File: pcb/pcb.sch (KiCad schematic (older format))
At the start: 19 parts

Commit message: Improved schematic
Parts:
- added C?: 100n, symbol Device:C
- added D?: D, symbol Device:D
- added J?: BAT+, symbol Connector:Conn_01x01_Male
- added J?: BAT-, symbol Connector:Conn_01x01_Male
- added R?: 330, symbol Device:R
- added R?: 2.7K, symbol Device:R
- added U?: AP9101CK6, symbol components:AP9101CK6
- added U?: DMN2053UVT, symbol components:DMN2053UVT
- C?: value C -> 22u
- C?: value C -> 100n
- J?: value Conn_01x06_Male -> AVR ISP connector
- J?: value Conn_01x02_Male -> I2C connector
- R? (x6): value R -> 10K
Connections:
- net labels added: GND_P
- net labels removed: +BATT
- wire segments 67 -> 92
- no-connect marks 21 -> 24
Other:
- note added: "AP9101CK6-AYTRG1"
- note added: "DMN2053UVT-7"
- moved on the sheet: C?, R?, SW?, U?

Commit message: Updated schematic and added gitignore for KiCAD files
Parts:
- removed BT?: Battery_Cell, symbol Device:Battery_Cell
- removed D?: LED, symbol Device:LED
- removed D?: D, symbol Device:D
- removed J?: I2C connector, symbol Connector:Conn_01x02_Male
- removed J?: BAT+, symbol Connector:Conn_01x01_Male
- removed J?: BAT-, symbol Connector:Conn_01x01_Male
- removed R? (x2): 10K, symbol Device:R
- removed R?: 2.7K, symbol Device:R
- removed U?: TP4056, symbol components:TP4056
- added C?: 4.7u, symbol Device:C
- added J?: Display connector, symbol Connector:Conn_01x08_Male
- added R? (x2): 2.7K, symbol Device:R
- added SW?: SW_DPDT_x2, symbol Switch:SW_DPDT_x2
- added U?: MCP73831-2-OT, symbol components:MCP73831-2-OT
- C?: value 22u -> 4.7u
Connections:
- net labels added: BAT+, BAT-, DISP_RST, VBACKUP
- net labels removed: GND_P
- wire segments 92 -> 89
- no-connect marks 24 -> 26
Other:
- note added: "// buttons\nPD3 (INT1) - BTN2\nPD2 (INT0) - BTN1\n\n// I²C bus\nPC5 (SCL) - SCL\nPC4 (SDA) - SDA\n\n// display\nPD0 - DISP_RST\n\n// SPI bus\nPB5 (SCK) - SCK\nPB4 (MISO) - MISO\nPB3 (MOSI) - MOSI\nPC6 (RESET#) - RESET\n"
- note added: "I_bat = 1000 / R_prog = 100 mA\nR_prog = 10 K"
- note removed: "// buttons\nPD3 (INT1) - BTN2\nPD2 (INT0) - BTN1\n\n// I²C bus\nPC5 (SCL) - SCL\nPC4 (SDA) - SDA\n\n// SPI bus\nPB5 (SCK) - SCK\nPB4 (MISO) - MISO\nPB3 (MOSI) - MOSI\nPC6 (RESET#) - RESET\n"
- note removed: "I_bat = 1200 / R_prog = 120 mA\nR_prog = 10 K"
- moved on the sheet: C?, D?, J?, R?, U?

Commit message: Added datasheets and push button footprint
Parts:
- removed SW? (x2): SW_Push, symbol Switch:SW_Push
- added SW2, SW3: SW_DIP_x01, symbol Switch:SW_DIP_x01
- U2: renamed from U?; footprint (none) -> pcb:MCP73831_SOT-23
- gave numbers to parts that had none: 20
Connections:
- net BTN1: now also SW2.1
- net BTN2: now also SW3.1
- net GND: now also SW2.2, SW3.2
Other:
- moved on the sheet: R4, R6

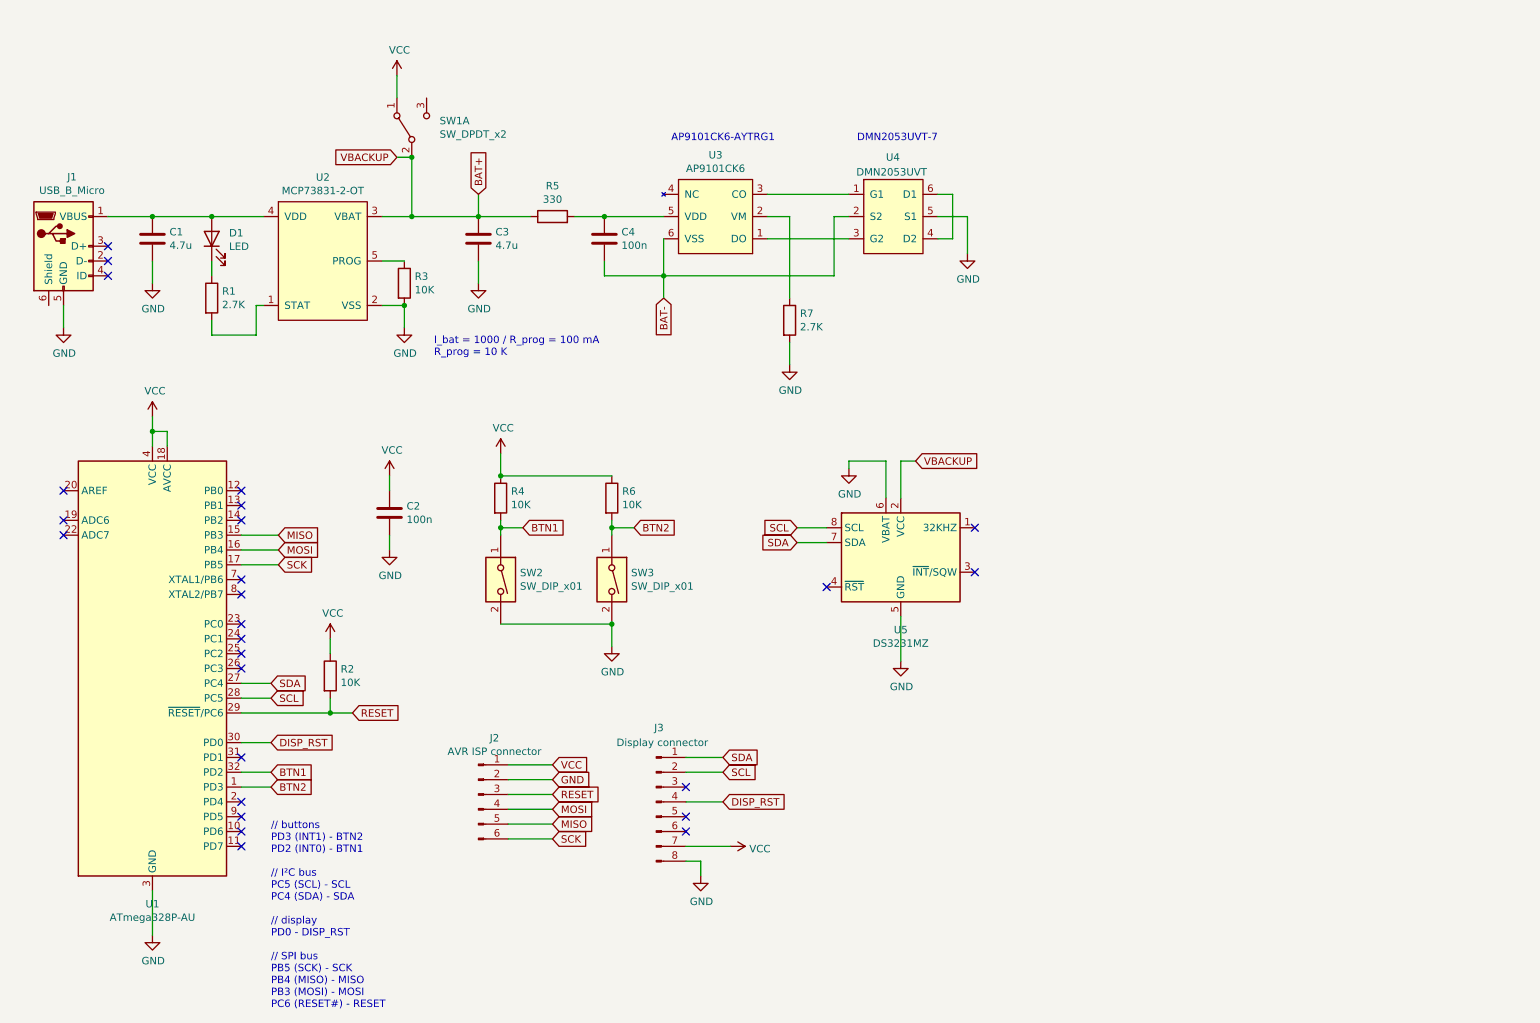
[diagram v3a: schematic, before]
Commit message: Updated footprints and schematic
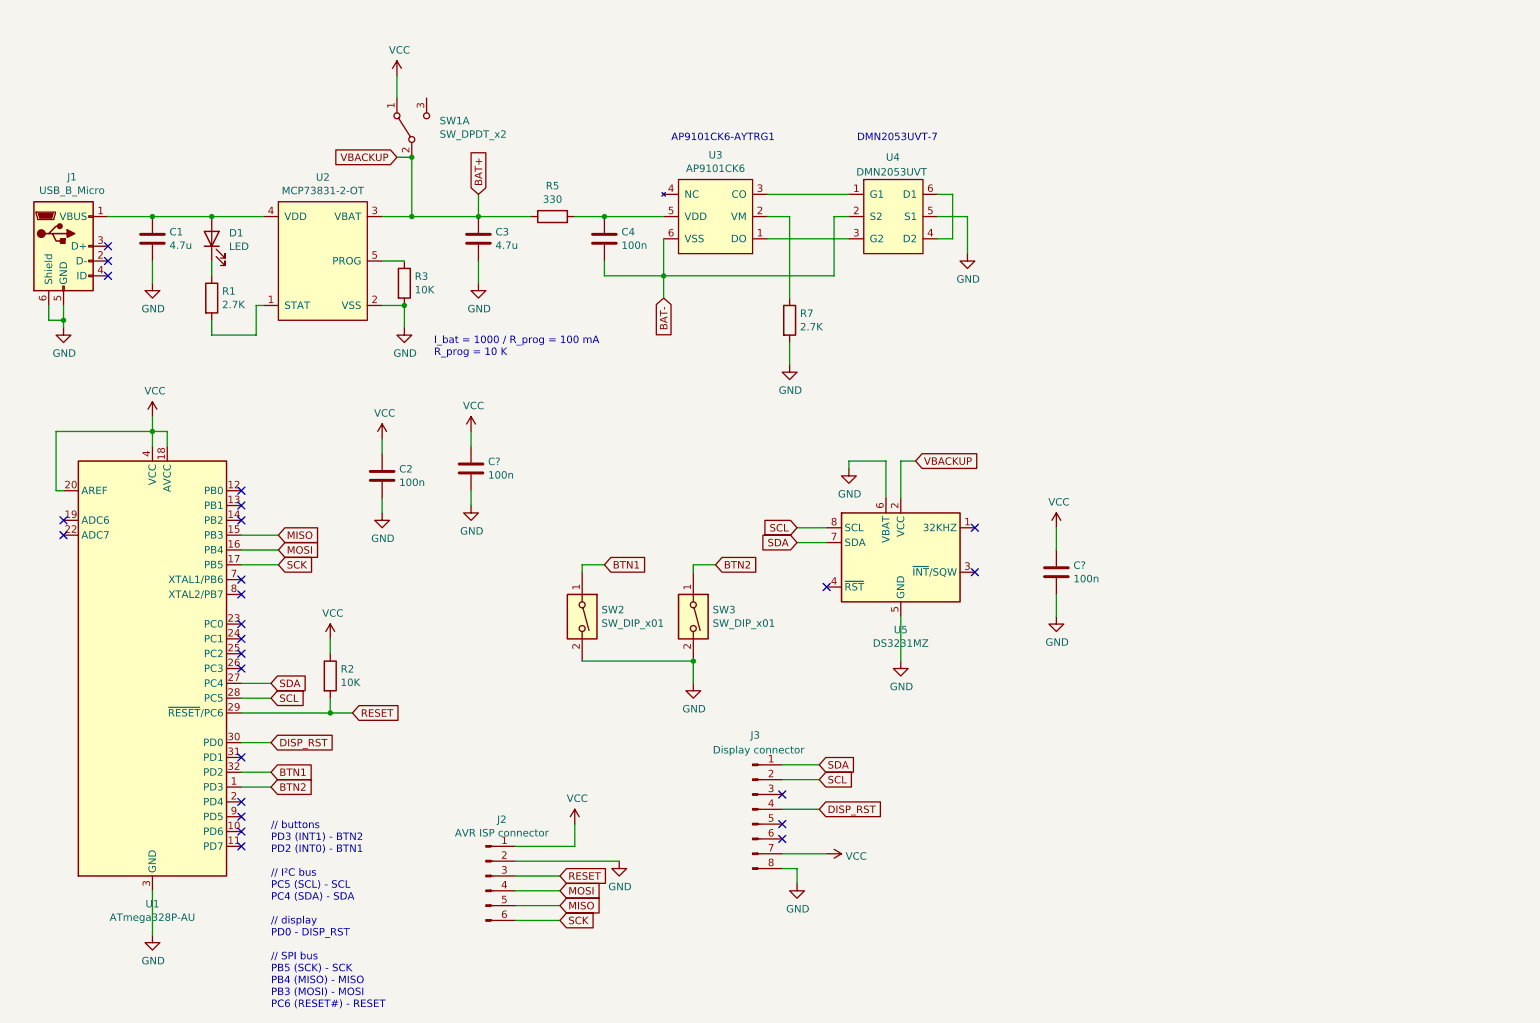
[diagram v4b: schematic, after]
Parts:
- removed R4, R6: 10K, symbol Device:R
- added C? (x2): 100n, Capacitor_SMD:C_0603_1608Metric, symbol Device:C
- C1, C2, C3, C4: footprint (none) -> Capacitor_SMD:C_0603_1608Metric
- D1: footprint (none) -> LED_SMD:LED_0805_2012Metric
- J1: footprint (none) -> pcb:USB_B_micro
- J2: footprint (none) -> pcb:CONN_AVR_ISP_SMD
- J3: footprint (none) -> Connector_PinHeader_2.54mm:PinHeader_1x08_P2.54mm_Vertical
- R1, R2, R3, R5, R7: footprint (none) -> Resistor_SMD:R_0603_1608Metric
- SW1: footprint (none) -> pcb:SW_3P
- SW2, SW3: footprint (none) -> pcb:TL3340_SMT
- U3: footprint (none) -> pcb:AP9101C_SOT-25
- U4: footprint (none) -> pcb:DMN2053UVT_TSOT-26
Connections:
- net GND: now also J1.6 (Shield), C?.2, C?.2
- net VCC: now also U1.20 (AREF), C?.1, C?.1
- no-connect marks 26 -> 25
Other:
- moved on the sheet: C2, J2, J3, SW2, SW3

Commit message: Finalized PCB layout
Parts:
- added J4: Conn_01x02_Male, Connector_JST:JST_PH_B2B-PH-K_1x02_P2.00mm_Vertical, symbol Connector:Conn_01x02_Male
- SW1: value SW_DPDT_x2 -> SSSS811101; footprint pcb:SW_3P -> pcb:SSSS811101
- gave numbers to parts that had none: 2
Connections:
- net BAT+: now also C6.1, J4.2 (Pin_2)
- net BAT-: now also J4.1 (Pin_1)
- net VCC: no longer C6.1
- no-connect marks 25 -> 26
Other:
- moved on the sheet: C6
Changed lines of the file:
@@
 P 3550 1450
 F 0 "SW1" V 3596 1262 50  0000 R CNN
-F 1 "SW_DPDT_x2" V 3505 1262 50  0000 R CNN
-F 2 "pcb:SW_3P" H 3550 1450 50  0001 C CNN
+F 1 "SSSS811101" V 3505 1262 50  0000 R CNN
+F 2 "pcb:SSSS811101" H 3550 1450 50  0001 C CNN
 F 3 "~" H 3550 1450 50  0001 C CNN
 	1    3550 1450
@@
 VBACKUP
 Wire Wire Line
-	6850 3700 6850 3950
+	6850 3700 6850 3850
 Wire Wire Line
 	6850 3700 6950 3700
@@
 Connection ~ 5450 5050
 $Comp
-L Device:C C?
+L Device:C C5
 U 1 1 5E7351D4
 P 3950 3750
-F 0 "C?" H 4065 3796 50  0000 L CNN
+F 0 "C5" H 4065 3796 50  0000 L CNN
 F 1 "100n" H 4065 3705 50  0000 L CNN
 F 2 "Capacitor_SMD:C_0603_1608Metric" H 3988 3600 50  0001 C CNN
@@
 $EndComp
 $Comp
-L power:VCC #PWR?
+L power:VCC #PWR0108
 U 1 1 5E73E851
 P 3950 3500
-F 0 "#PWR?" H 3950 3350 50  0001 C CNN
+F 0 "#PWR0108" H 3950 3350 50  0001 C CNN
 F 1 "VCC" H 3967 3673 50  0000 C CNN
 F 2 "" H 3950 3500 50  0001 C CNN
@@
 $EndComp
 $Comp
-L power:GND #PWR?
+L power:GND #PWR0119
 U 1 1 5E73EC60
 P 3950 4000
-F 0 "#PWR?" H 3950 3750 50  0001 C CNN
+F 0 "#PWR0119" H 3950 3750 50  0001 C CNN
 F 1 "GND" H 3955 3827 50  0000 C CNN
 F 2 "" H 3950 4000 50  0001 C CNN
@@
 	1150 3900 1200 3900
 $Comp
-L Device:C C?
+L Device:C C6
 U 1 1 5E760DB3
-P 7900 4450
-F 0 "C?" H 8015 4496 50  0000 L CNN
-F 1 "100n" H 8015 4405 50  0000 L CNN
-F 2 "Capacitor_SMD:C_0603_1608Metric" H 7938 4300 50  0001 C CNN
-F 3 "~" H 7900 4450 50  0001 C CNN
-	1    7900 4450
-	1    0    0    -1
-$EndComp
-$Comp
-L power:VCC #PWR?
-U 1 1 5E7611A7
-P 7900 4150
-F 0 "#PWR?" H 7900 4000 50  0001 C CNN
-F 1 "VCC" H 7917 4323 50  0000 C CNN
-F 2 "" H 7900 4150 50  0001 C CNN
-F 3 "" H 7900 4150 50  0001 C CNN
-	1    7900 4150
-	1    0    0    -1
-$EndComp
-$Comp
-L power:GND #PWR?
+P 7850 4150
+F 0 "C6" H 7965 4196 50  0000 L CNN
+F 1 "100n" H 7965 4105 50  0000 L CNN
+F 2 "Capacitor_SMD:C_0603_1608Metric" H 7888 4000 50  0001 C CNN
+F 3 "~" H 7850 4150 50  0001 C CNN
+	1    7850 4150
+	1    0    0    -1
+$EndComp
+$Comp
+L power:GND #PWR0121
 U 1 1 5E7615E0
-P 7900 4750
-F 0 "#PWR?" H 7900 4500 50  0001 C CNN
-F 1 "GND" H 7905 4577 50  0000 C CNN
-F 2 "" H 7900 4750 50  0001 C CNN
-F 3 "" H 7900 4750 50  0001 C CNN
-	1    7900 4750
-	1    0    0    -1
-$EndComp
-Wire Wire Line
-	7900 4600 7900 4750
-Wire Wire Line
-	7900 4300 7900 4150
+P 7850 4450
+F 0 "#PWR0121" H 7850 4200 50  0001 C CNN
+F 1 "GND" H 7855 4277 50  0000 C CNN
+F 2 "" H 7850 4450 50  0001 C CNN
+F 3 "" H 7850 4450 50  0001 C CNN
+	1    7850 4450
+	1    0    0    -1
+$EndComp
+Wire Wire Line
+	7850 4300 7850 4450
+Wire Wire Line
+	7850 4000 7850 3850
 Wire Wire Line
 	1100 2650 1100 2750
@@
 	1200 2750 1200 2800
 $Comp
-L power:VCC #PWR?
+L power:VCC #PWR0122
 U 1 1 5E77F285
 P 4650 6150
-F 0 "#PWR?" H 4650 6000 50  0001 C CNN
+F 0 "#PWR0122" H 4650 6000 50  0001 C CNN
 F 1 "VCC" H 4667 6323 50  0000 C CNN
 F 2 "" H 4650 6150 50  0001 C CNN
@@
 	4250 6300 4650 6300
 $Comp
-L power:GND #PWR?
+L power:GND #PWR0123
 U 1 1 5E782845
 P 4950 6400
-F 0 "#PWR?" H 4950 6150 50  0001 C CNN
+F 0 "#PWR0123" H 4950 6150 50  0001 C CNN
 F 1 "GND" H 4955 6227 50  0000 C CNN
 F 2 "" H 4950 6400 50  0001 C CNN
@@
 Wire Wire Line
 	4250 6400 4950 6400
+NoConn ~ 3650 1250
+$Comp
+L Connector:Conn_01x02_Male J4
+U 1 1 5E792C70
+P 1700 1450
+F 0 "J4" H 1808 1631 50  0000 C CNN
+F 1 "Conn_01x02_Male" H 1808 1540 50  0000 C CNN
+F 2 "Connector_JST:JST_PH_B2B-PH-K_1x02_P2.00mm_Vertical" H 1700 1450 50  0001 C CNN
+F 3 "~" H 1700 1450 50  0001 C CNN
+	1    1700 1450
+	1    0    0    -1
+$EndComp
+Text GLabel 2050 1550 2    50   Input ~ 0
+BAT+
+Text GLabel 2050 1450 2    50   Input ~ 0
+BAT-
+Wire Wire Line
+	2050 1450 1900 1450
+Wire Wire Line
+	1900 1550 2050 1550
+Wire Wire Line
+	6850 3850 7850 3850
+Connection ~ 6850 3850
+Wire Wire Line
+	6850 3850 6850 3950
 $EndSCHEMATC

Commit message: Finalized schematic and PCB layout
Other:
- note added: "https://www.conrad.de/de/p/b2b-ph-k-s-lf-sn-connector-header-male-pitch2mm-top-entry-2p-th-inhalt-20-stueck-800113239.html"
- moved on the sheet: J4
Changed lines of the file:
@@
 L Connector:Conn_01x02_Male J4
 U 1 1 5E792C70
-P 1700 1450
-F 0 "J4" H 1808 1631 50  0000 C CNN
-F 1 "Conn_01x02_Male" H 1808 1540 50  0000 C CNN
-F 2 "Connector_JST:JST_PH_B2B-PH-K_1x02_P2.00mm_Vertical" H 1700 1450 50  0001 C CNN
-F 3 "~" H 1700 1450 50  0001 C CNN
-	1    1700 1450
+P 1800 1350
+F 0 "J4" H 1908 1531 50  0000 C CNN
+F 1 "Conn_01x02_Male" H 1908 1440 50  0000 C CNN
+F 2 "Connector_JST:JST_PH_B2B-PH-K_1x02_P2.00mm_Vertical" H 1800 1350 50  0001 C CNN
+F 3 "~" H 1800 1350 50  0001 C CNN
+	1    1800 1350
 	1    0    0    -1
 $EndComp
-Text GLabel 2050 1550 2    50   Input ~ 0
+Text GLabel 2150 1450 2    50   Input ~ 0
 BAT+
-Text GLabel 2050 1450 2    50   Input ~ 0
+Text GLabel 2150 1350 2    50   Input ~ 0
 BAT-
 Wire Wire Line
-	2050 1450 1900 1450
+	2150 1350 2000 1350
 Wire Wire Line
-	1900 1550 2050 1550
+	2000 1450 2150 1450
 Wire Wire Line
 	6850 3850 7850 3850
@@
 Wire Wire Line
 	6850 3850 6850 3950
+Text Notes 850  1600 0    50   ~ 0
+https://www.conrad.de/de/p/b2b-ph-k-s-lf-sn-connector-header-male-pitch2mm-top-entry-2p-th-inhalt-20-stueck-800113239.html
 $EndSCHEMATC
